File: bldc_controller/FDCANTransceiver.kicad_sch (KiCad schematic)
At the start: 4 parts, among them U9 TCAN1051HGVDRBRQ1

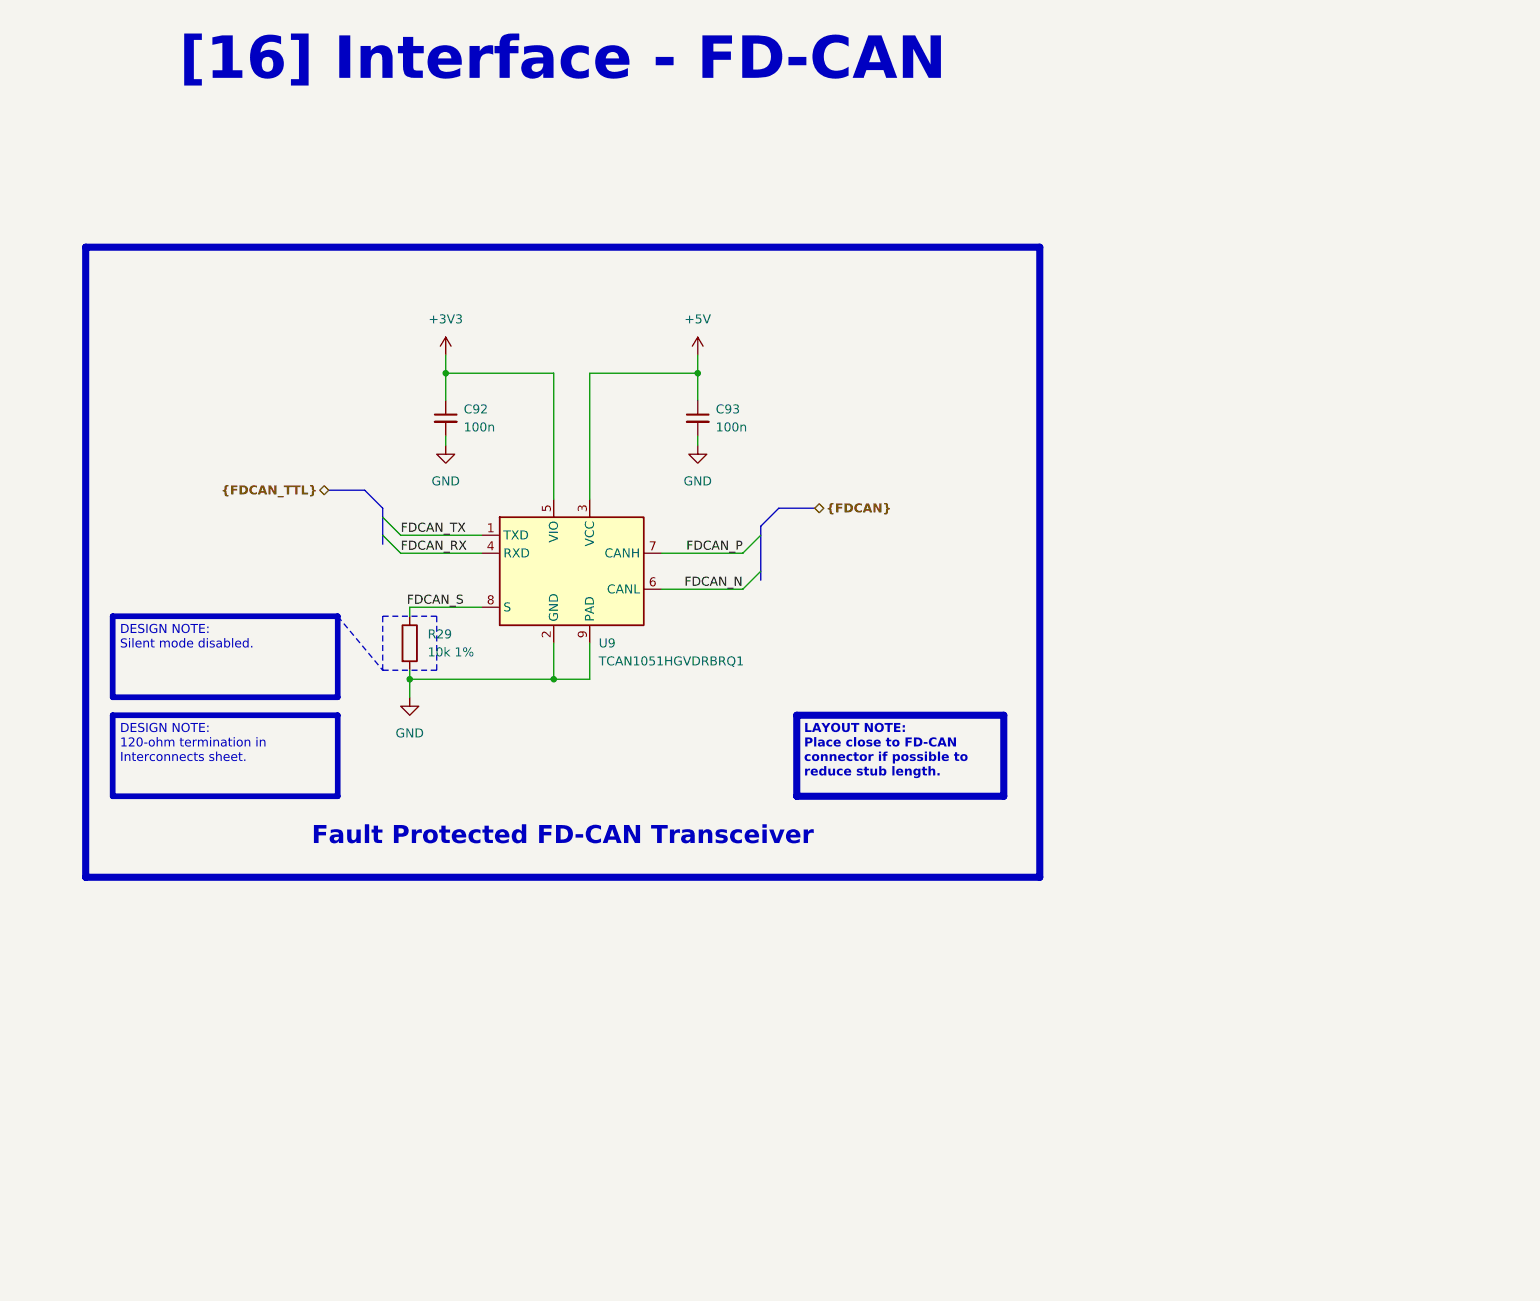
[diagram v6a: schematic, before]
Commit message: Replaced 3v3 buck with WSON package alternative. Will back-annotate components
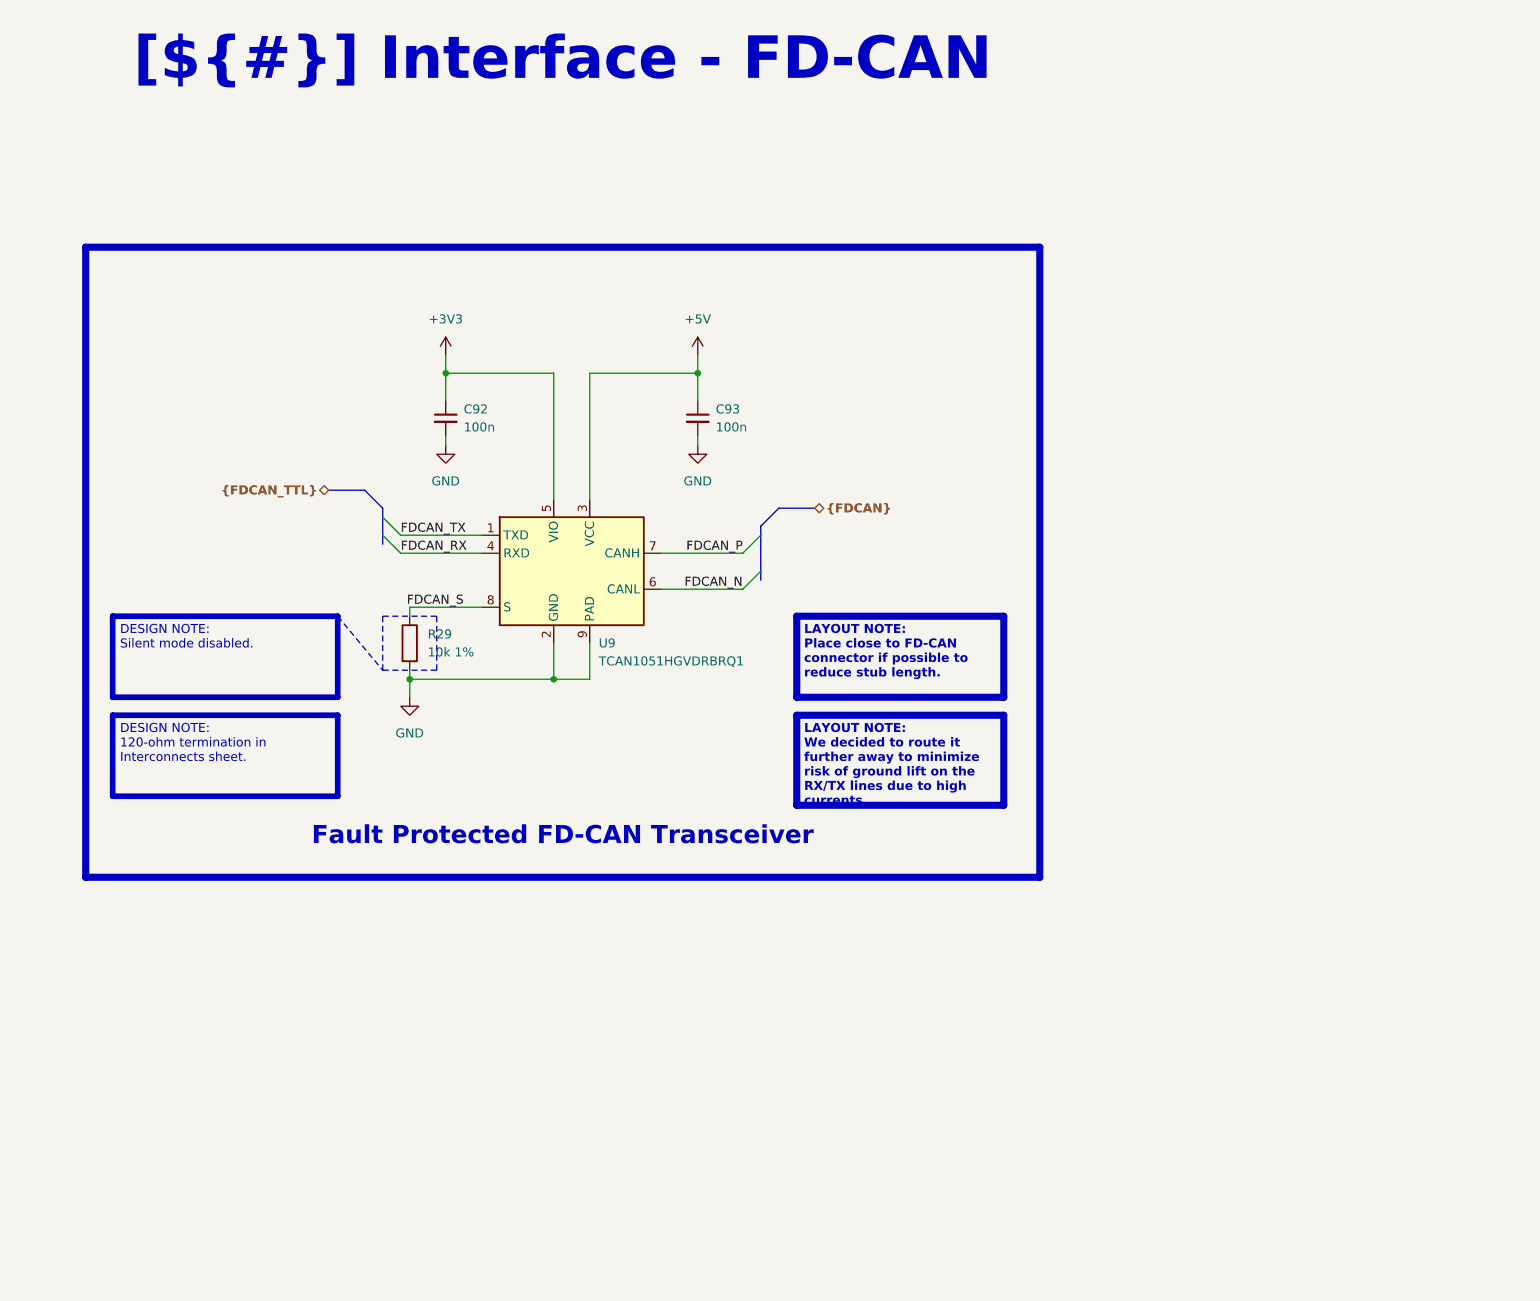
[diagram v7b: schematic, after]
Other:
- company: EPFL Xplore -> ${COMPANY}
- title: FD-CAN Transceiver -> Interface - FD-CAN
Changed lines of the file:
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@@
   (paper "A4")
   (title_block
-    (title "FD-CAN Transceiver")
+    (title "Interface - FD-CAN")
     (date "2023-10-15")
-    (rev "1.0")
-    (company "EPFL Xplore")
-    (comment 3 "Author: Vincent Nguyen")
+    (rev "${REVISION}")
+    (company "${COMPANY}")
+    (comment 3 "Author: ${AUTHOR}")
   )
   (junction (at 132.08 67.31) (diameter 0) (color 0 0 0 0)
   )
-  (junction (at 147.32 110.49) (diameter 0) (color 0 0 0 1)
+  (junction (at 147.32 110.49) (diameter 0) (color 0 0 0 0)
   )
   (junction (at 167.64 67.31) (diameter 0) (color 0 0 0 0)
   )
-  (junction (at 127 110.49) (diameter 0) (color 0 0 0 1)
+  (junction (at 127 110.49) (diameter 0) (color 0 0 0 0)
   )
   (bus_entry (at 176.53 95.25) (size -2.54 2.54)
@@
   )
   (wire (pts (xy 127 110.49) (xy 147.32 110.49))
-    (stroke (width 0.381) (type default) (color 0 0 0 1))
+    (stroke (width 0) (type default))
   )
   (bus (pts (xy 176.53 90.17) (xy 176.53 95.25))
@@
   )
   (wire (pts (xy 147.32 110.49) (xy 152.4 110.49))
-    (stroke (width 0.381) (type default) (color 0 0 0 1))
+    (stroke (width 0) (type default))
   )
   (bus (pts (xy 176.53 95.25) (xy 176.53 96.52))
@@
   )
   (wire (pts (xy 132.08 77.47) (xy 132.08 76.2))
-    (stroke (width 0.381) (type default) (color 0 0 0 1))
+    (stroke (width 0) (type default))
   )
   (wire (pts (xy 152.4 67.31) (xy 152.4 85.09))
@@
   )
   (wire (pts (xy 147.32 105.41) (xy 147.32 110.49))
-    (stroke (width 0.381) (type default) (color 0 0 0 1))
+    (stroke (width 0) (type default))
   )
   (wire (pts (xy 132.08 71.12) (xy 132.08 67.31))
@@
   )
   (wire (pts (xy 167.64 77.47) (xy 167.64 76.2))
-    (stroke (width 0.381) (type default) (color 0 0 0 1))
+    (stroke (width 0) (type default))
   )
   (bus (pts (xy 123.19 90.17) (xy 123.19 91.44))
@@
   )
   (wire (pts (xy 127 113.03) (xy 127 110.49))
-    (stroke (width 0.381) (type default) (color 0 0 0 1))
+    (stroke (width 0) (type default))
   )
   (wire (pts (xy 127 109.22) (xy 127 110.49))
-    (stroke (width 0.381) (type default) (color 0 0 0 1))
+    (stroke (width 0) (type default))
   )
   (wire (pts (xy 152.4 110.49) (xy 152.4 105.41))
-    (stroke (width 0.381) (type default) (color 0 0 0 1))
+    (stroke (width 0) (type default))
   )
   (wire (pts (xy 132.08 64.77) (xy 132.08 67.31))
@@
   )
   (text_box "LAYOUT NOTE:\nPlace close to FD-CAN connector if possible to reduce stub length."
-    (at 181.61 115.57 0) (size 29.21 11.43)
+    (at 181.61 101.6 0) (size 29.21 11.43)
+    (stroke (width 1) (type solid) (color 0 0 255 1))
+    (fill (type none))
+    (effects (font (face "Arial") (size 1.27 1.27) (thickness 0.4) bold (color 0 0 255 1)) (justify left top))
+  )
+  (text_box "LAYOUT NOTE:\nWe decided to route it further away to minimize risk of ground lift on the RX/TX lines due to high currents."
+    (at 181.61 115.57 0) (size 29.21 12.7)
     (stroke (width 1) (type solid) (color 0 0 255 1))
     (fill (type none))
@@
     (effects (font (face "Arial") (size 1.27 1.27) (color 0 0 0 1)) (justify left top))
   )
-  (text_box "[16] Interface - FD-CAN"
+  (text_box "[${#}] ${TITLE}"
     (at 80.01 16.51 0) (size 137.16 12.7)
     (stroke (width -0.0001) (type default))

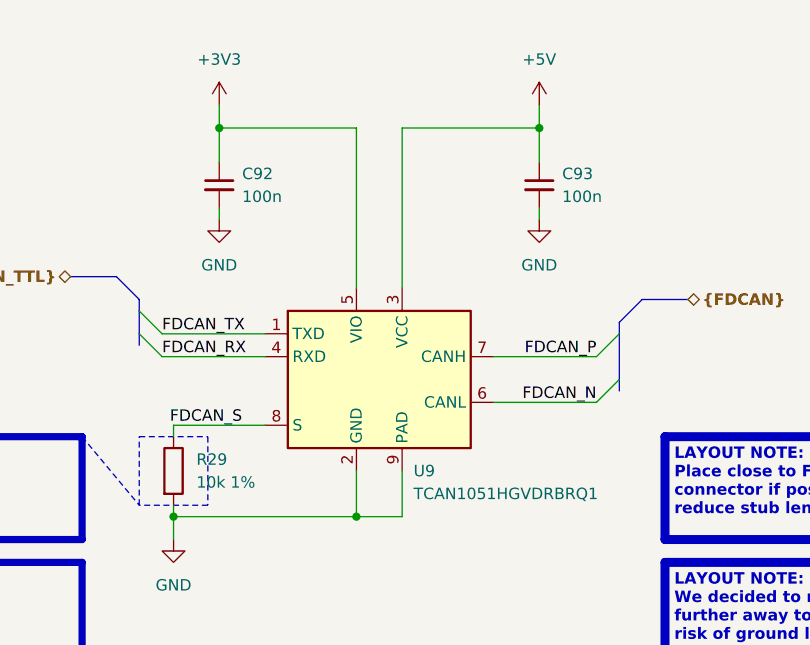
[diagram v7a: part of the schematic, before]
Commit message: routed all signals. TODO: redo all power polygons and ensure good return paths/reference. Added 3d models
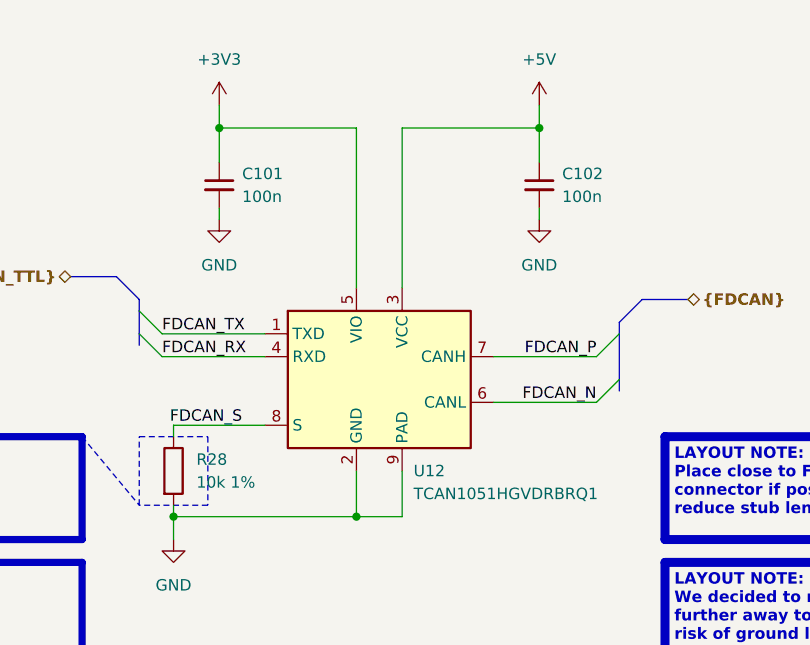
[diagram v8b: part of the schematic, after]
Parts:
- renumbered C92 to C101, C93 to C102, R29 to R28, U9 to U12
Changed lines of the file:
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@@
   (symbol (lib_id "0_interface_can:TCAN1051HGVDRBRQ1") (at 149.86 95.25 0) (unit 1)
     (in_bom yes) (on_board yes) (dnp no)
-    (property "Reference" "U9" (at 153.67 105.41 0)
+    (property "Reference" "U12" (at 153.67 105.41 0)
       (effects (font (size 1.27 1.27)) (justify left))
     )
@@
       (project "bldc_controller"
         (path "/0650c7a8-acba-429c-9f8e-eec0baf0bc1c/fede4c36-00cc-4d3d-b71c-5243ba232202/95bf33d9-762c-4d08-af8b-3fad797ffaca"
-          (reference "U9") (unit 1)
+          (reference "U12") (unit 1)
         )
       )
@@
   (symbol (lib_id "power:+3V3") (at 132.08 64.77 0) (unit 1)
     (in_bom yes) (on_board yes) (dnp no) (fields_autoplaced)
-    (property "Reference" "#PWR053" (at 132.08 68.58 0)
+    (property "Reference" "#PWR054" (at 132.08 68.58 0)
       (effects (font (size 1.27 1.27)) hide)
     )
@@
       (project "bldc_controller"
         (path "/0650c7a8-acba-429c-9f8e-eec0baf0bc1c/fede4c36-00cc-4d3d-b71c-5243ba232202/95bf33d9-762c-4d08-af8b-3fad797ffaca"
+          (reference "#PWR054") (unit 1)
+        )
+      )
+    )
+  )
+  (symbol (lib_id "power:GND") (at 127 113.03 0) (unit 1)
+    (in_bom yes) (on_board yes) (dnp no) (fields_autoplaced)
+    (property "Reference" "#PWR053" (at 127 119.38 0)
+      (effects (font (size 1.27 1.27)) hide)
+    )
+    (property "Value" "GND" (at 127 118.11 0)
+      (effects (font (size 1.27 1.27)))
+    )
+    (property "Footprint" "" (at 127 113.03 0)
+      (effects (font (size 1.27 1.27)) hide)
+    )
+    (property "Datasheet" "" (at 127 113.03 0)
+      (effects (font (size 1.27 1.27)) hide)
+    )
+    (pin "1")
+    (instances
+      (project "bldc_controller"
+        (path "/0650c7a8-acba-429c-9f8e-eec0baf0bc1c/fede4c36-00cc-4d3d-b71c-5243ba232202/95bf33d9-762c-4d08-af8b-3fad797ffaca"
           (reference "#PWR053") (unit 1)
-        )
-      )
-    )
-  )
-  (symbol (lib_id "power:GND") (at 127 113.03 0) (unit 1)
-    (in_bom yes) (on_board yes) (dnp no) (fields_autoplaced)
-    (property "Reference" "#PWR052" (at 127 119.38 0)
-      (effects (font (size 1.27 1.27)) hide)
-    )
-    (property "Value" "GND" (at 127 118.11 0)
-      (effects (font (size 1.27 1.27)))
-    )
-    (property "Footprint" "" (at 127 113.03 0)
-      (effects (font (size 1.27 1.27)) hide)
-    )
-    (property "Datasheet" "" (at 127 113.03 0)
-      (effects (font (size 1.27 1.27)) hide)
-    )
-    (pin "1")
-    (instances
-      (project "bldc_controller"
-        (path "/0650c7a8-acba-429c-9f8e-eec0baf0bc1c/fede4c36-00cc-4d3d-b71c-5243ba232202/95bf33d9-762c-4d08-af8b-3fad797ffaca"
-          (reference "#PWR052") (unit 1)
         )
       )
@@
   (symbol (lib_id "power:GND") (at 132.08 77.47 0) (unit 1)
     (in_bom yes) (on_board yes) (dnp no)
-    (property "Reference" "#PWR054" (at 132.08 83.82 0)
+    (property "Reference" "#PWR055" (at 132.08 83.82 0)
       (effects (font (size 1.27 1.27)) hide)
     )
@@
       (project "bldc_controller"
         (path "/0650c7a8-acba-429c-9f8e-eec0baf0bc1c/fede4c36-00cc-4d3d-b71c-5243ba232202/95bf33d9-762c-4d08-af8b-3fad797ffaca"
-          (reference "#PWR054") (unit 1)
+          (reference "#PWR055") (unit 1)
         )
       )
@@
   (symbol (lib_id "power:GND") (at 167.64 77.47 0) (mirror y) (unit 1)
     (in_bom yes) (on_board yes) (dnp no) (fields_autoplaced)
-    (property "Reference" "#PWR056" (at 167.64 83.82 0)
+    (property "Reference" "#PWR057" (at 167.64 83.82 0)
       (effects (font (size 1.27 1.27)) hide)
     )
@@
       (project "bldc_controller"
         (path "/0650c7a8-acba-429c-9f8e-eec0baf0bc1c/fede4c36-00cc-4d3d-b71c-5243ba232202/95bf33d9-762c-4d08-af8b-3fad797ffaca"
-          (reference "#PWR056") (unit 1)
+          (reference "#PWR057") (unit 1)
         )
       )
@@
   (symbol (lib_id "Device:C_Small") (at 167.64 73.66 0) (unit 1)
     (in_bom yes) (on_board yes) (dnp no)
-    (property "Reference" "C93" (at 170.18 72.3963 0)
+    (property "Reference" "C102" (at 170.18 72.3963 0)
       (effects (font (size 1.27 1.27)) (justify left))
     )
@@
       (project "bldc_controller"
         (path "/0650c7a8-acba-429c-9f8e-eec0baf0bc1c/fede4c36-00cc-4d3d-b71c-5243ba232202/95bf33d9-762c-4d08-af8b-3fad797ffaca"
-          (reference "C93") (unit 1)
+          (reference "C102") (unit 1)
         )
       )
@@
   (symbol (lib_id "power:+5V") (at 167.64 64.77 0) (unit 1)
     (in_bom yes) (on_board yes) (dnp no) (fields_autoplaced)
-    (property "Reference" "#PWR055" (at 167.64 68.58 0)
+    (property "Reference" "#PWR056" (at 167.64 68.58 0)
       (effects (font (size 1.27 1.27)) hide)
     )
@@
       (project "bldc_controller"
         (path "/0650c7a8-acba-429c-9f8e-eec0baf0bc1c/fede4c36-00cc-4d3d-b71c-5243ba232202/95bf33d9-762c-4d08-af8b-3fad797ffaca"
-          (reference "#PWR055") (unit 1)
+          (reference "#PWR056") (unit 1)
         )
       )
@@
   (symbol (lib_id "Device:C_Small") (at 132.08 73.66 0) (unit 1)
     (in_bom yes) (on_board yes) (dnp no) (fields_autoplaced)
-    (property "Reference" "C92" (at 134.62 72.3963 0)
+    (property "Reference" "C101" (at 134.62 72.3963 0)
       (effects (font (size 1.27 1.27)) (justify left))
     )
@@
       (project "bldc_controller"
         (path "/0650c7a8-acba-429c-9f8e-eec0baf0bc1c/fede4c36-00cc-4d3d-b71c-5243ba232202/95bf33d9-762c-4d08-af8b-3fad797ffaca"
-          (reference "C92") (unit 1)
+          (reference "C101") (unit 1)
         )
       )
@@
   (symbol (lib_id "Device:R") (at 127 105.41 0) (unit 1)
     (in_bom yes) (on_board yes) (dnp no) (fields_autoplaced)
-    (property "Reference" "R29" (at 129.54 104.14 0)
+    (property "Reference" "R28" (at 129.54 104.14 0)
       (effects (font (size 1.27 1.27)) (justify left))
     )
@@
       (project "bldc_controller"
         (path "/0650c7a8-acba-429c-9f8e-eec0baf0bc1c/fede4c36-00cc-4d3d-b71c-5243ba232202/95bf33d9-762c-4d08-af8b-3fad797ffaca"
-          (reference "R29") (unit 1)
-        )
-      )
+          (reference "R28") (unit 1)
+        )
+      )
